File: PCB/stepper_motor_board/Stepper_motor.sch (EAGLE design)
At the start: 27 parts, among them U1 A4988_STEPPER_MOTOR_DRIVER_CA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, U2 A4988_STEPPER_MOTOR_DRIVER_CA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, U3 A4988_STEPPER_MOTOR_DRIVER_CA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

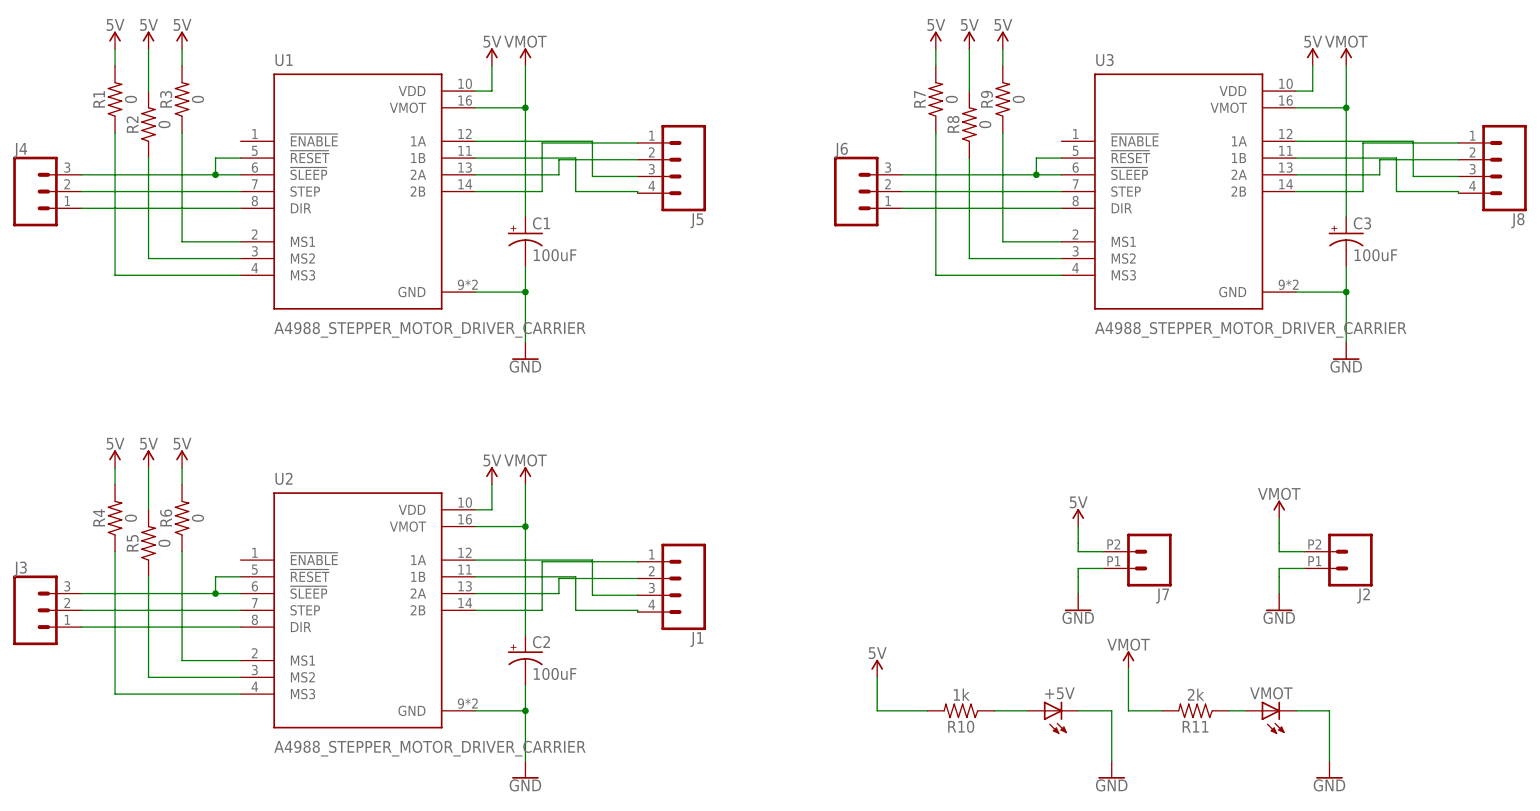
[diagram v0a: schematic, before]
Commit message: new version of stepper pcb and lighthouse pcb
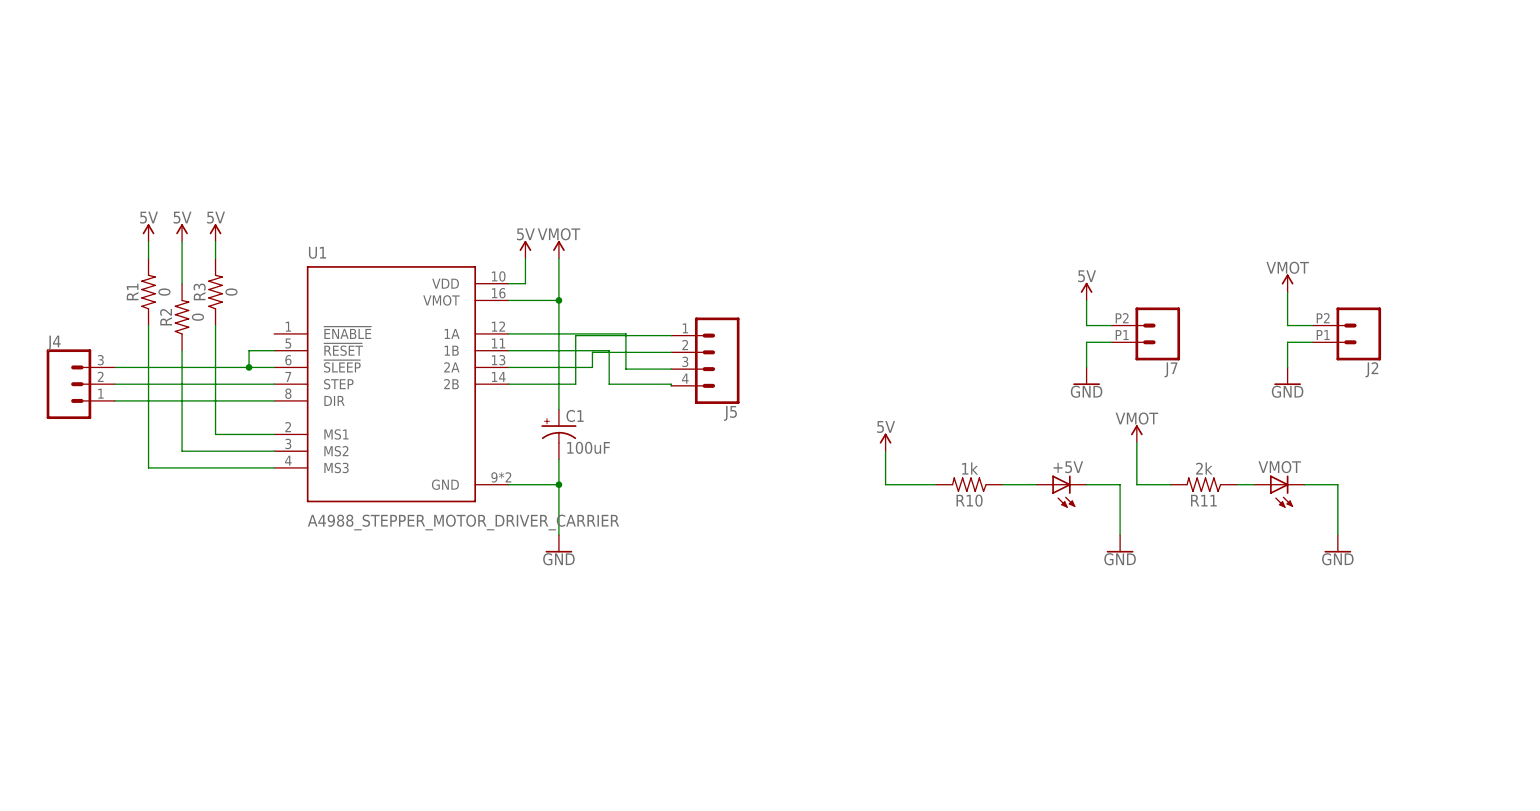
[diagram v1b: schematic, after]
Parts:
- removed C2, C3: 100uF, SparkFun-Capacitors:100UF-POLAR-25V-20%(ELEC)
- removed J1, J8: (no value), SparkFun-Connectors:CONN_04JST-PTH-VERT
- removed J3, J6: (no value), SparkFun-Connectors:CONN_03SCREW
- removed R4, R5, R6, R7, R8, R9: 0, SparkFun-Resistors:RESISTOR1206
- removed U2, U3: A4988_STEPPER_MOTOR_DRIVER_CARRIER, A4988_STEPPER_MOTOR_DRIVER_CARRIER:A4988_STEPPER_MOTOR_DRIVER_CARRIER
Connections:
- removed net N$15: J3.2, U2.STEP
- removed net N$16: J3.1, U2.DIR
- removed net N$17: J3.3, U2.!RESET, U2.!SLEEP
- removed net N$18: R6.1, U2.MS1
- removed net N$19: R5.1, U2.MS2
- removed net N$20: R4.1, U2.MS3
- removed net N$25: J6.2, U3.STEP
- removed net N$26: J6.1, U3.DIR
- removed net N$27: J6.3, U3.!RESET, U3.!SLEEP
- removed net N$28: R9.1, U3.MS1
- removed net N$29: R8.1, U3.MS2
- removed net N$30: R7.1, U3.MS3
- removed net N$31: J8.4, U3.1B
- removed net N$32: J8.3, U3.1A
- removed net N$33: J8.2, U3.2A
- removed net N$34: J8.1, U3.2B
- removed net N$35: J1.4, U2.1B
- removed net N$36: J1.3, U2.1A
- removed net N$37: J1.2, U2.2A
- removed net N$38: J1.1, U2.2B
- net 12V: no longer C2.+, C3.+, U2.VMOT, U3.VMOT
- net 5V: no longer R4.2, R5.2, R6.2, R7.2, R8.2, R9.2, U2.VDD, U3.VDD
- net GND: no longer C2.-, C3.-, U2.GND, U3.GND
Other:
- moved on the sheet: +5V, C1, J2, J4, J5, J7, R1, R10, R11, R2, R3, U1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

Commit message: update pcb for order
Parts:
- removed J5: (no value), SparkFun-Connectors:CONN_04JST-PTH-VERT
- removed J7: (no value), SparkFun-Connectors:CONN_02SCREWTERMINAL-6.35MM-2
- added J1: (no value), SparkFun-Connectors:CONN_025MM
- added J3: B4B-XH-A(LF)(SN), B4B-XH-A_LF__SN_:B4B-XH-A(LF)(SN)
- J2: device SparkFun-Connectors:CONN_02SCREWTERMINAL-6.35MM-2 -> SparkFun-Connectors:CONN_025MM
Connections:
- net 12V: now also J2.2; no longer J2.1
- net 5V: now also J1.2; no longer J7.1
- net GND: now also J1.1, J2.1; no longer J2.2, J7.2
- net N$1: now also J3.1; no longer J5.4
- net N$2: now also J3.2; no longer J5.3
- net N$3: now also J3.3; no longer J5.2
- net N$4: now also J3.4; no longer J5.1
- net N$6: now also J4.3; no longer J4.1
- net N$7: now also J4.1; no longer J4.3
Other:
- moved on the sheet: J2, J4
